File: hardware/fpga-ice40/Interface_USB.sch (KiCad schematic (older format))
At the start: 12 parts, among them J5 USB_B_Micro, U9 FT245RL

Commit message: Completed verification of all pins for all symbols
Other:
- moved on the sheet: C20, J5, R2
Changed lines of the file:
@@
 AR Path="/5F314850" Ref="U?"  Part="1"
 AR Path="/5F302051/5F314850" Ref="U9"  Part="1"
-F 0 "U9" H 6975 4315 50  0000 C CNN
-F 1 "FT245RL" H 6975 4224 50  0000 C CNN
+F 0 "U9" H 6350 4300 50  0000 L CNN
+F 1 "FT245RL" H 6350 4200 50  0000 L CNN
 F 2 "Package_SO:SSOP-28_5.3x10.2mm_P0.65mm" H 6500 4200 50  0001 C CNN
 F 3 "https://www.ftdichip.com/Support/Documents/DataSheets/ICs/DS_FT245R.pdf" H 6500 4200 50  0001 C CNN
@@
 Text GLabel 4200 4350 0    50   UnSpc ~ 0
 USB_5V
-Connection ~ 3800 3450
 $Comp
 L ng_conn:USB_B_Micro J?
 U 1 1 5F314899
-P 2850 3650
+P 2750 3650
 AR Path="/5F314899" Ref="J?"  Part="1"
 AR Path="/5F302051/5F314899" Ref="J5"  Part="1"
-F 0 "J5" H 2907 4117 50  0000 C CNN
-F 1 "USB_B_Micro" H 2907 4026 50  0000 C CNN
-F 2 "Connector_USB:USB_Micro-B_Molex_47346-0001" H 3000 3650 50  0001 C CNN
-F 3 "~" H 3000 3650 50  0001 C CNN
-F 4 "47346-0001" H 2850 3650 50  0001 C CNN "MPN"
-	1    2850 3650
-	1    0    0    -1
-$EndComp
-Text Label 2750 4400 1    50   ~ 0
+F 0 "J5" H 2550 4100 50  0000 L CNN
+F 1 "USB_B_Micro" H 2550 4000 50  0000 L CNN
+F 2 "Connector_USB:USB_Micro-B_Molex_47346-0001" H 2900 3650 50  0001 C CNN
+F 3 "https://www.molex.com/pdm_docs/sd/473460001_sd.pdf" H 2900 3650 50  0001 C CNN
+F 4 "47346-0001" H 2750 3650 50  0001 C CNN "MPN"
+	1    2750 3650
+	1    0    0    -1
+$EndComp
+Text Label 2650 4400 1    50   ~ 0
 USB_SHD
-Connection ~ 2750 4250
-Wire Wire Line
-	2750 4450 2750 4250
-Wire Wire Line
-	2850 4450 2750 4450
-Wire Wire Line
-	2750 4250 2750 4050
-Wire Wire Line
-	2850 4250 2750 4250
-Wire Wire Line
-	3250 4450 3250 4550
-Connection ~ 3250 4450
-Wire Wire Line
-	3150 4450 3250 4450
-Wire Wire Line
-	3250 4250 3250 4450
-Connection ~ 3250 4250
-Wire Wire Line
-	3150 4250 3250 4250
+Connection ~ 2650 4250
+Wire Wire Line
+	2650 4450 2650 4250
+Wire Wire Line
+	2750 4450 2650 4450
+Wire Wire Line
+	2650 4250 2650 4050
+Wire Wire Line
+	2750 4250 2650 4250
+Wire Wire Line
+	3150 4450 3150 4550
+Connection ~ 3150 4450
+Wire Wire Line
+	3050 4450 3150 4450
+Wire Wire Line
+	3150 4250 3150 4450
+Connection ~ 3150 4250
+Wire Wire Line
+	3050 4250 3150 4250
 $Comp
 L Device:C C?
 U 1 1 5F314906
-P 3000 4450
+P 2900 4450
 AR Path="/5F314906" Ref="C?"  Part="1"
 AR Path="/5F302051/5F314906" Ref="C20"  Part="1"
-F 0 "C20" V 2850 4450 50  0000 C CNN
-F 1 "10n" V 2750 4450 50  0000 C CNN
-F 2 "Capacitor_SMD:C_0603_1608Metric" H 3038 4300 50  0001 C CNN
-F 3 "~" H 3000 4450 50  0001 C CNN
-F 4 "CL10B103KC8NNNC" H 3000 4450 50  0001 C CNN "MPN"
-	1    3000 4450
+F 0 "C20" V 2750 4450 50  0000 C CNN
+F 1 "10n" V 2650 4450 50  0000 C CNN
+F 2 "Capacitor_SMD:C_0603_1608Metric" H 2938 4300 50  0001 C CNN
+F 3 "~" H 2900 4450 50  0001 C CNN
+F 4 "CL10B103KC8NNNC" H 2900 4450 50  0001 C CNN "MPN"
+	1    2900 4450
 	0    -1   -1   0
 $EndComp
@@
 L Device:R R?
 U 1 1 5F314900
-P 3000 4250
+P 2900 4250
 AR Path="/5F314900" Ref="R?"  Part="1"
 AR Path="/5F302051/5F314900" Ref="R2"  Part="1"
-F 0 "R2" V 2800 4250 50  0000 C CNN
-F 1 "100k" V 2900 4250 50  0000 C CNN
-F 2 "Resistor_SMD:R_0603_1608Metric" V 2930 4250 50  0001 C CNN
-F 3 "~" H 3000 4250 50  0001 C CNN
-F 4 "RC0603JR-07100KL" H 3000 4250 50  0001 C CNN "MPN"
-	1    3000 4250
+F 0 "R2" V 2700 4250 50  0000 C CNN
+F 1 "100k" V 2800 4250 50  0000 C CNN
+F 2 "Resistor_SMD:R_0603_1608Metric" V 2830 4250 50  0001 C CNN
+F 3 "~" H 2900 4250 50  0001 C CNN
+F 4 "RC0603JR-07100KL" H 2900 4250 50  0001 C CNN "MPN"
+	1    2900 4250
 	0    1    1    0
 $EndComp
-Text Label 3250 3450 0    50   ~ 0
-USB_VBUS
-Text GLabel 3250 3650 2    50   Input ~ 0
+Text GLabel 3150 3650 2    50   Input ~ 0
 USB_D+
-Text GLabel 3250 3550 2    50   Input ~ 0
+Text GLabel 3150 3550 2    50   Input ~ 0
 USB_D-
 $Comp
 L ng_power:GND #PWR?
 U 1 1 5F3148A5
-P 3250 4550
+P 3150 4550
 AR Path="/5F3148A5" Ref="#PWR?"  Part="1"
 AR Path="/5F302051/5F3148A5" Ref="#PWR023"  Part="1"
-F 0 "#PWR023" H 3250 4300 50  0001 C CNN
-F 1 "GND" H 3253 4424 50  0000 C CNN
-F 2 "" H 3150 4200 50  0001 C CNN
-F 3 "" H 3250 4550 50  0001 C CNN
-	1    3250 4550
-	1    0    0    -1
-$EndComp
-Wire Wire Line
-	3150 3650 3250 3650
-Wire Wire Line
-	3150 3550 3250 3550
-Wire Wire Line
-	3150 3450 3800 3450
-Wire Wire Line
-	3250 3850 3250 4250
-Wire Wire Line
-	3150 3850 3250 3850
-NoConn ~ 3150 3750
+F 0 "#PWR023" H 3150 4300 50  0001 C CNN
+F 1 "GND" H 3153 4424 50  0000 C CNN
+F 2 "" H 3050 4200 50  0001 C CNN
+F 3 "" H 3150 4550 50  0001 C CNN
+	1    3150 4550
+	1    0    0    -1
+$EndComp
+Wire Wire Line
+	3050 3650 3150 3650
+Wire Wire Line
+	3050 3550 3150 3550
+Wire Wire Line
+	3050 3450 3800 3450
+Wire Wire Line
+	3150 3850 3150 4250
+Wire Wire Line
+	3050 3850 3150 3850
+NoConn ~ 3050 3750
+Connection ~ 3800 3450
+Text Label 3150 3450 0    50   ~ 0
+USB_VBUS
 $EndSCHEMATC

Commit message: Completed schematic review
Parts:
- C19: value 100n -> 4u7; MPN CL10B104KB8NNNC -> CL10A475KA8NQNC
- R3: value 10k -> 6k8; MPN RC0603FR-0710KL -> RC0603FR-076K8L
- R5: value 20k -> 10k; MPN RC0603JR-0720KL -> RC0603FR-0710KL
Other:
- note added: "USB_DETn < 3.3V\nfor compatibility\nwith FPGA IO bank"
- moved on the sheet: C18, C19, C20, C21, C22, FB1, J5, R2, R3, R4, R5, U9

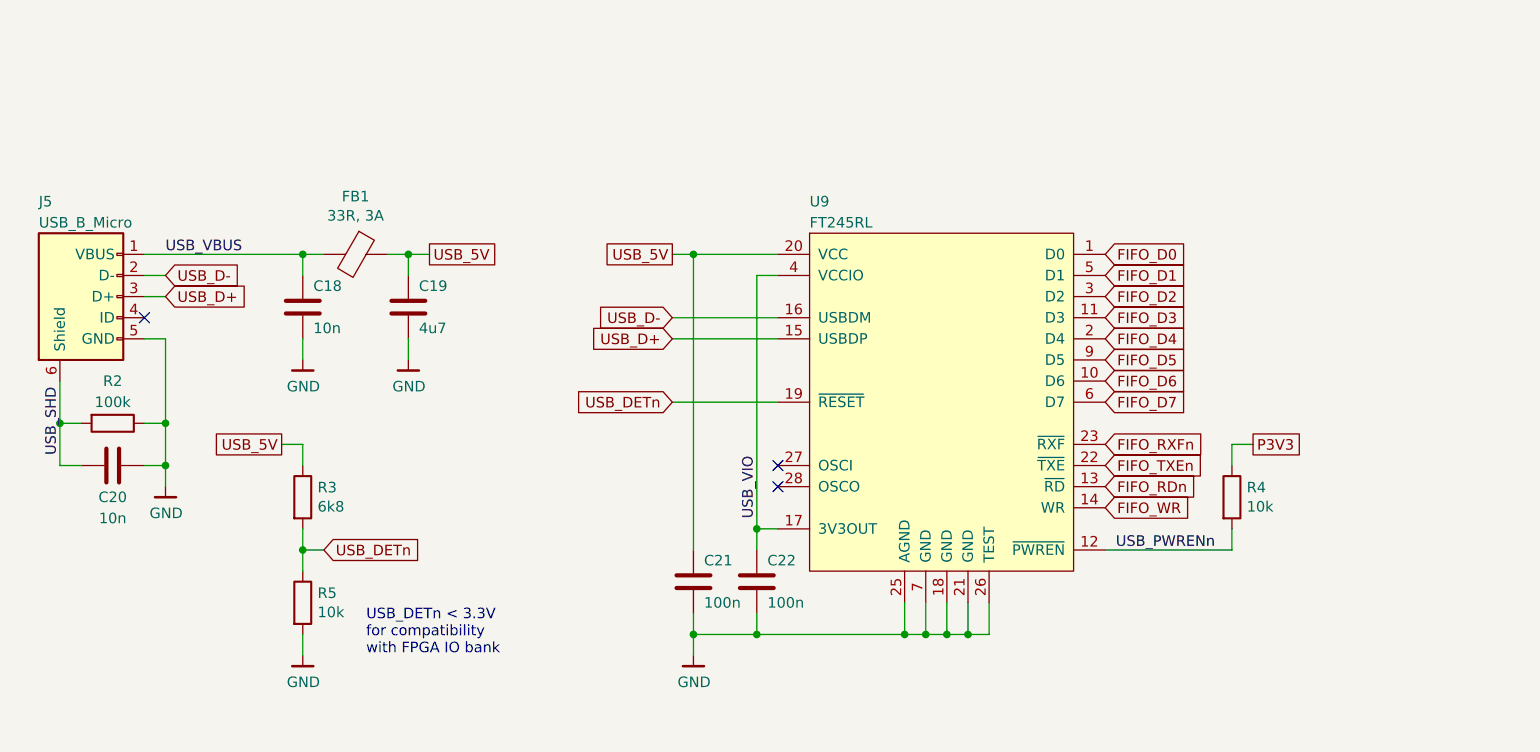
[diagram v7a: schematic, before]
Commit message: Fix mechanical issue by moving USB connector to top of board
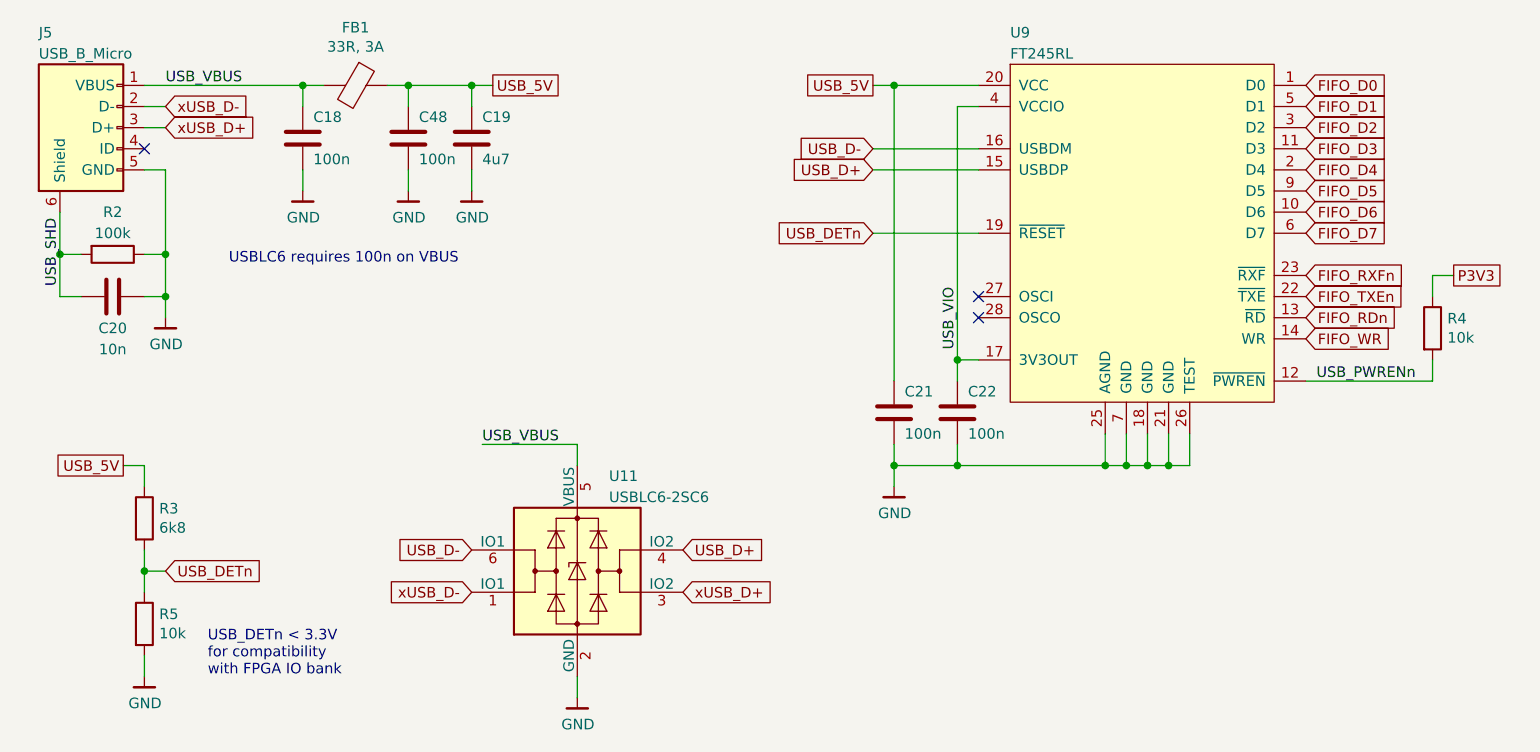
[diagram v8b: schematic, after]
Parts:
- added C48: 100n, Capacitor_SMD:C_0603_1608Metric, symbol Device:C
- added U11: USBLC6-2SC6, Package_TO_SOT_SMD:SOT-23-6, symbol Power_Protection:USBLC6-2SC6
- C18: value 10n -> 100n; MPN CL10B103KC8NNNC -> CL10B104KB8NNNC
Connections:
- net GND: now also C48.2, U11.2 (GND)
- net USB_5V: now also C48.1
- net USB_D+: now also U11.4 (IO2); no longer J5.3 (D+)
- net USB_D-: now also U11.6 (IO1); no longer J5.2 (D-)
- net USB_VBUS: now also U11.5 (VBUS)
- new net xUSB_D+: J5.3 (D+), U11.3 (IO2)
- new net xUSB_D-: J5.2 (D-), U11.1 (IO1)
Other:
- note added: "USBLC6 requires 100n on VBUS"
- moved on the sheet: C18, C19, C20, C21, C22, FB1, J5, R2, R3, R4, R5, U9
